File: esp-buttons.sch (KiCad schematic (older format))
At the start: 41 parts, among them CON1 POWER_5V, P1 CONN_BUTTON1, P2 CONN_BUTTON2, P3 CONN_BUTTON3, P4 CONN_BUTTON4, P5 CONN_BUTTON5, P6 UART_DEBUG, P7 UART, P8 POWER_5V, P9 USB, Q1 IRLML2502TRPBF, Q2 IRLML2502TRPBF, Q3 IRLML2502TRPBF, Q4 IRLML2502TRPBF, Q5 IRLML2502TRPBF, SW1 RESET_BUTTON, SW2 PROG_BUTTON, U1 ESP-07v2, U2 LD1117S33CTR, U3 FT230XS

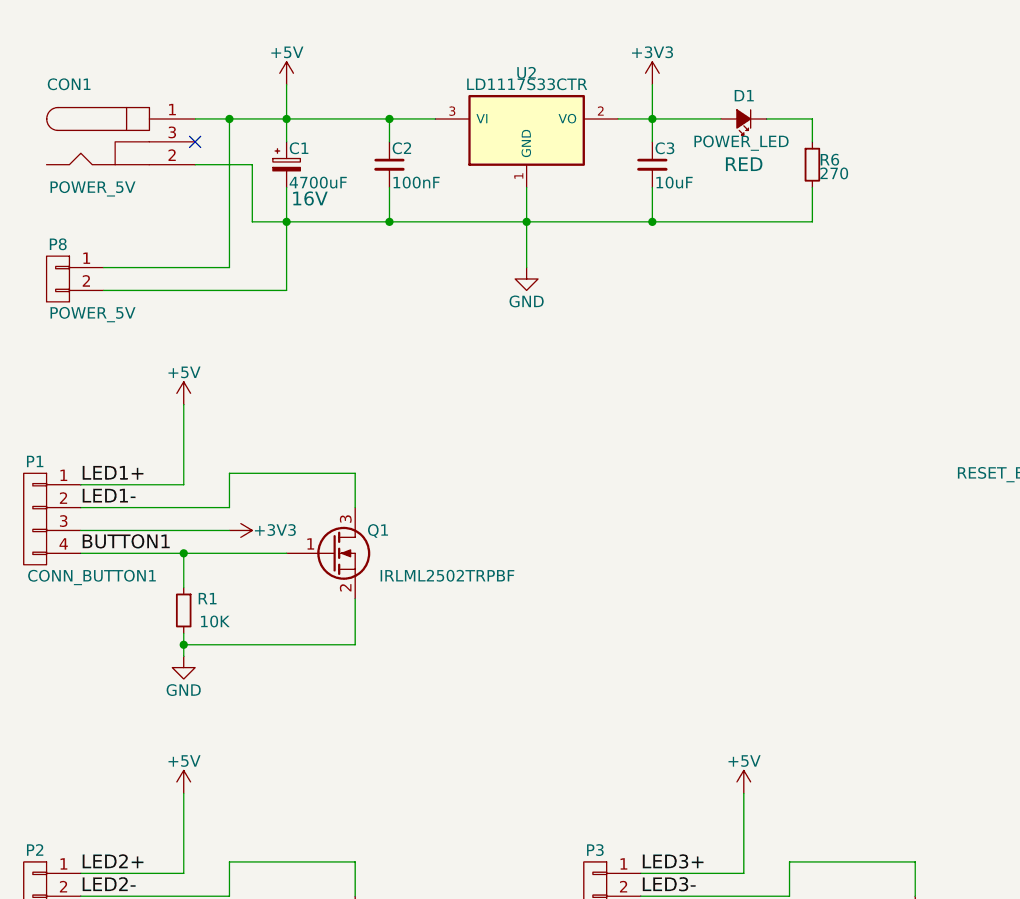
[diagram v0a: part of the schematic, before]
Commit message: Fixed some ERC warnings with the PWR_FLAG
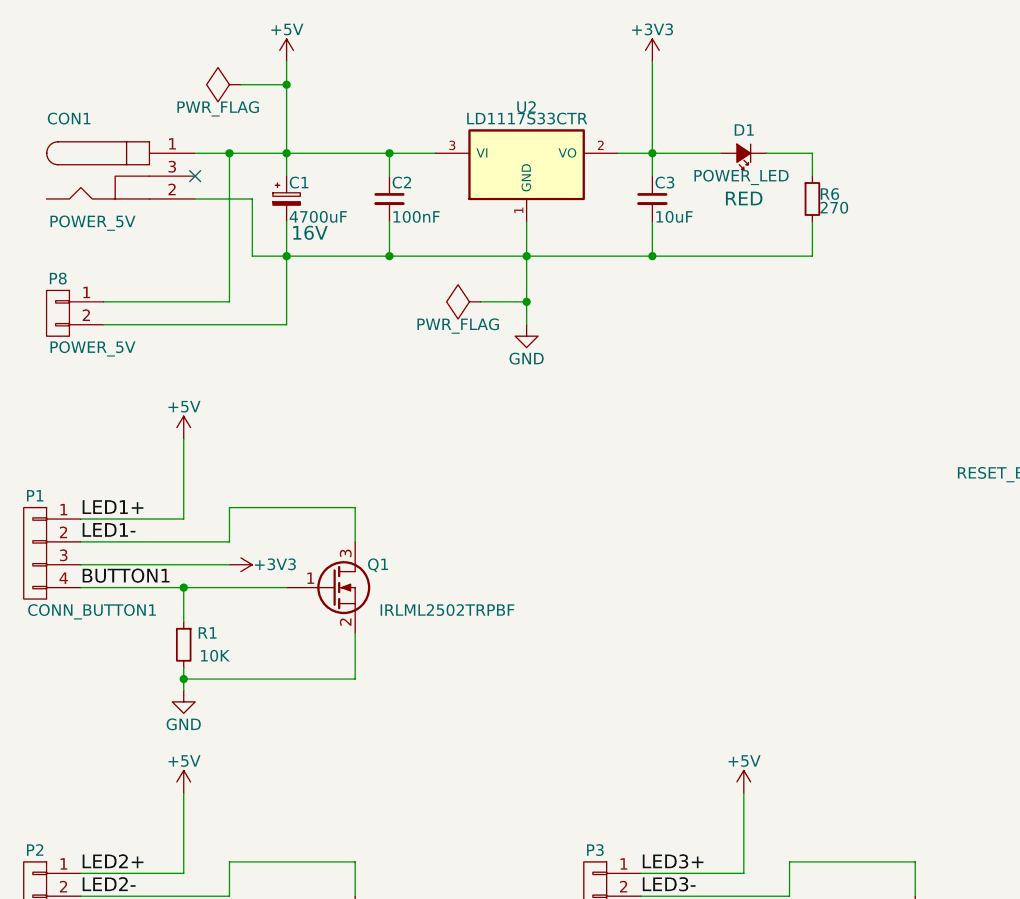
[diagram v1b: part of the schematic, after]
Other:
- moved on the sheet: C1, C2, C3, CON1, D1, P1, P8, Q1, R1, R6, U2

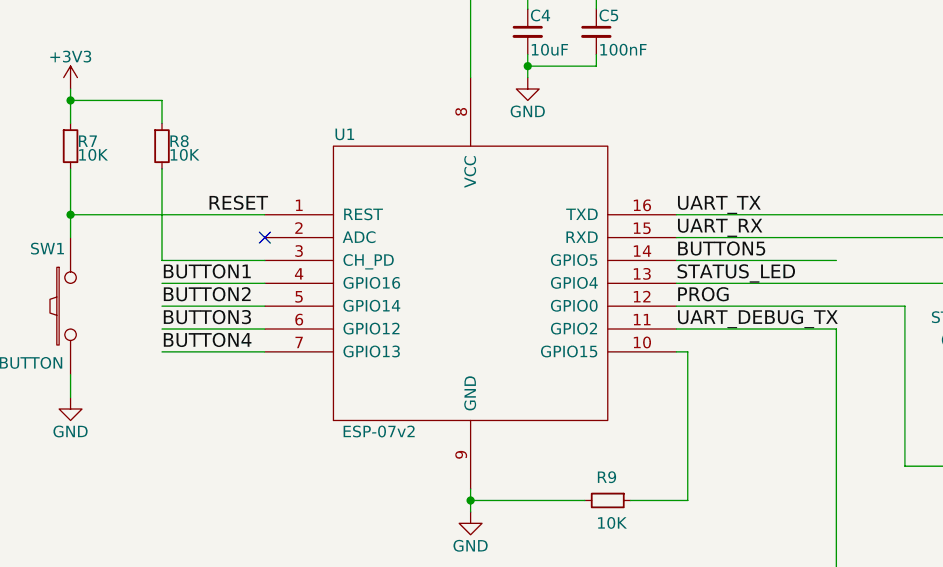
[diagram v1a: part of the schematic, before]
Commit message: More component placement and track layout done. Exchanged the connections of two buttons on the ESP's pins
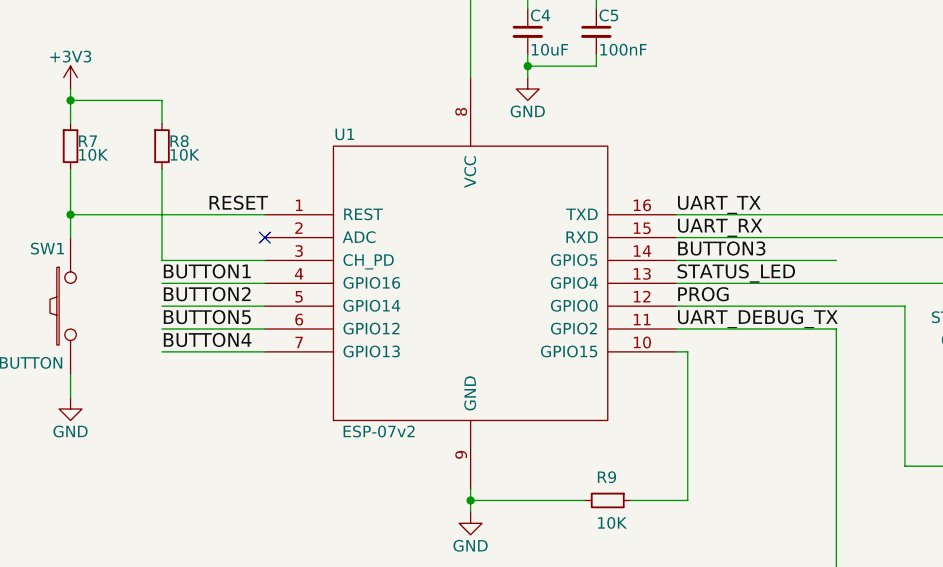
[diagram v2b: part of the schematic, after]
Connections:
- net BUTTON3: now also U1.14 (GPIO5); no longer U1.6 (GPIO12)
- net BUTTON5: now also U1.6 (GPIO12); no longer U1.14 (GPIO5)
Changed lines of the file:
@@
 Text Label 7850 2250 0    60   ~ 0
 PROG
-Text Label 7850 2050 0    60   ~ 0
+Text Label 5600 2350 0    60   ~ 0
 BUTTON5
 $Comp
@@
 Text Label 5600 2250 0    60   ~ 0
 BUTTON2
-Text Label 5600 2350 0    60   ~ 0
+Text Label 7850 2050 0    60   ~ 0
 BUTTON3
 Text Label 5600 2450 0    60   ~ 0
